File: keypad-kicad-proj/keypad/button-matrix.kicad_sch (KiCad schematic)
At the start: 36 parts, among them SW1 Cherry_MX, SW10 Cherry_MX, SW11 Cherry_MX, SW12 Cherry_MX, SW13 SW_SPST, SW14 SW_SPST, SW15 SW_SPST, SW16 SW_SPST, SW17 SW_SPST, SW18 SW_SPST, SW19 SW_SPST, SW2 Cherry_MX, SW20 SW_SPST, SW21 SW_SPST, SW22 SW_SPST, SW23 SW_SPST, SW24 SW_SPST, SW3 Cherry_MX, SW4 Cherry_MX, SW5 Cherry_MX, SW6 Cherry_MX, SW7 Cherry_MX, SW8 Cherry_MX, SW9 Cherry_MX

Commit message: rest of the schematic
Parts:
- renumbered D2 to D28, D6 to D29, D10 to D30, D3 to D31, D7 to D32, D11 to D33, D4 to D34, D8 to D35, D12 to D36, D5 to D37, D9 to D38, D13 to D39, SW1 to SW26, SW5 to SW27, SW9 to SW28, SW13 to SW29, SW15 to SW30, SW21 to SW31, SW2 to SW32, SW6 to SW33, SW10 to SW34, SW14 to SW35, SW16 to SW36, SW20 to SW37, SW3 to SW38, SW7 to SW39, SW11 to SW40, SW17 to SW41, SW18 to SW42, SW19 to SW43, SW4 to SW44, SW8 to SW45, SW12 to SW46, SW24 to SW47, SW23 to SW48, SW22 to SW49
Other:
- note added: "Button matrix (4x3)"
- title: (none) -> Keypad board
- moved on the sheet: D28, D29, D30, D31, D32, D33, D34, D35, D36, D37, D38, D39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

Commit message: keypad update
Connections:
- net Col_0 renamed col_0
- net Col_1 renamed col_1
- net Col_2 renamed col_2
- net Col_3 renamed col_3
- net Row_0 renamed row_0
- net Row_1 renamed row_1
- net Row_2 renamed row_2
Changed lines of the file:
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@@
     (effects (font (size 3 3) (thickness 0.6) bold) (justify left bottom))
   )
-  (global_label "Row_2" (shape input) (at 73.66 118.11 180) (fields_autoplaced)
+  (global_label "row_2" (shape input) (at 73.66 118.11 180) (fields_autoplaced)
     (effects (font (size 1.27 1.27)) (justify right))
-    (property "Intersheetrefs" "${INTERSHEET_REFS}" (at 64.7482 118.11 0)
+    (property "Intersheetrefs" "${INTERSHEET_REFS}" (at 65.232 118.11 0)
       (effects (font (size 1.27 1.27)) (justify right) hide)
     )
   )
-  (global_label "Col_3" (shape input) (at 226.06 54.61 0) (fields_autoplaced)
+  (global_label "col_3" (shape output) (at 226.06 54.61 0) (fields_autoplaced)
     (effects (font (size 1.27 1.27)) (justify left))
-    (property "Intersheetrefs" "${INTERSHEET_REFS}" (at 234.3065 54.61 0)
+    (property "Intersheetrefs" "${INTERSHEET_REFS}" (at 234.1251 54.61 0)
       (effects (font (size 1.27 1.27)) (justify left) hide)
     )
   )
-  (global_label "Col_2" (shape input) (at 187.96 54.61 0) (fields_autoplaced)
+  (global_label "col_2" (shape output) (at 187.96 54.61 0) (fields_autoplaced)
     (effects (font (size 1.27 1.27)) (justify left))
-    (property "Intersheetrefs" "${INTERSHEET_REFS}" (at 196.2065 54.61 0)
+    (property "Intersheetrefs" "${INTERSHEET_REFS}" (at 196.0251 54.61 0)
       (effects (font (size 1.27 1.27)) (justify left) hide)
     )
   )
-  (global_label "Row_1" (shape input) (at 73.66 90.17 180) (fields_autoplaced)
+  (global_label "row_1" (shape input) (at 73.66 90.17 180) (fields_autoplaced)
     (effects (font (size 1.27 1.27)) (justify right))
-    (property "Intersheetrefs" "${INTERSHEET_REFS}" (at 64.7482 90.17 0)
+    (property "Intersheetrefs" "${INTERSHEET_REFS}" (at 65.232 90.17 0)
       (effects (font (size 1.27 1.27)) (justify right) hide)
     )
   )
-  (global_label "Row_0" (shape input) (at 73.66 60.96 180) (fields_autoplaced)
+  (global_label "row_0" (shape input) (at 73.66 60.96 180) (fields_autoplaced)
     (effects (font (size 1.27 1.27)) (justify right))
-    (property "Intersheetrefs" "${INTERSHEET_REFS}" (at 64.7482 60.96 0)
+    (property "Intersheetrefs" "${INTERSHEET_REFS}" (at 65.232 60.96 0)
       (effects (font (size 1.27 1.27)) (justify right) hide)
     )
   )
-  (global_label "Col_1" (shape input) (at 148.59 54.61 0) (fields_autoplaced)
+  (global_label "col_1" (shape output) (at 148.59 54.61 0) (fields_autoplaced)
     (effects (font (size 1.27 1.27)) (justify left))
-    (property "Intersheetrefs" "${INTERSHEET_REFS}" (at 156.8365 54.61 0)
+    (property "Intersheetrefs" "${INTERSHEET_REFS}" (at 156.6551 54.61 0)
       (effects (font (size 1.27 1.27)) (justify left) hide)
     )
   )
-  (global_label "Col_0" (shape input) (at 109.22 54.61 0) (fields_autoplaced)
+  (global_label "col_0" (shape output) (at 109.22 54.61 0) (fields_autoplaced)
     (effects (font (size 1.27 1.27)) (justify left))
-    (property "Intersheetrefs" "${INTERSHEET_REFS}" (at 117.4665 54.61 0)
+    (property "Intersheetrefs" "${INTERSHEET_REFS}" (at 117.2851 54.61 0)
       (effects (font (size 1.27 1.27)) (justify left) hide)
     )

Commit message: footprints
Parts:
- D28, D29, D30, D31, D32, D33, D34, D35, D36, D37, D38, D39: footprint (none) -> Diode_SMD:D_SOD-123
- SW26, SW27, SW28, SW32, SW33, SW34, SW38, SW39, SW40, SW44, SW45, SW46: footprint SW_MX1A-E1NW_CHY -> PUT_RocketLab_other:MX1A-E1NW cherry mx blue rgb
- SW29, SW30, SW31, SW35, SW36, SW37, SW41, SW42, SW43, SW47, SW48, SW49: footprint (none) -> Button_Switch_THT:SW_PUSH-12mm_Wuerth-430476085716
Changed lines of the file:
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@@
       (effects (font (size 1.524 1.524)))
     )
-    (property "Footprint" "SW_MX1A-E1NW_CHY" (at 88.9 106.299 0)
+    (property "Footprint" "PUT_RocketLab_other:MX1A-E1NW cherry mx blue rgb" (at 88.9 106.299 0)
       (effects (font (size 1.524 1.524)) hide)
     )
@@
       (effects (font (size 1.524 1.524)))
     )
-    (property "Footprint" "SW_MX1A-E1NW_CHY" (at 205.74 106.299 0)
+    (property "Footprint" "PUT_RocketLab_other:MX1A-E1NW cherry mx blue rgb" (at 205.74 106.299 0)
       (effects (font (size 1.524 1.524)) hide)
     )
@@
       (effects (font (size 1.27 1.27)))
     )
-    (property "Footprint" "" (at 140.97 129.54 90)
+    (property "Footprint" "Diode_SMD:D_SOD-123" (at 140.97 129.54 90)
       (effects (font (size 1.27 1.27)) hide)
     )
@@
       (effects (font (size 1.27 1.27)))
     )
-    (property "Footprint" "" (at 88.9 138.43 0)
+    (property "Footprint" "Button_Switch_THT:SW_PUSH-12mm_Wuerth-430476085716" (at 88.9 138.43 0)
       (effects (font (size 1.27 1.27)) hide)
     )
@@
       (effects (font (size 1.27 1.27)))
     )
-    (property "Footprint" "" (at 205.74 110.49 0)
+    (property "Footprint" "Button_Switch_THT:SW_PUSH-12mm_Wuerth-430476085716" (at 205.74 110.49 0)
       (effects (font (size 1.27 1.27)) hide)
     )
@@
       (effects (font (size 1.27 1.27)))
     )
-    (property "Footprint" "" (at 167.64 138.43 0)
+    (property "Footprint" "Button_Switch_THT:SW_PUSH-12mm_Wuerth-430476085716" (at 167.64 138.43 0)
       (effects (font (size 1.27 1.27)) hide)
     )
@@
       (effects (font (size 1.524 1.524)))
     )
-    (property "Footprint" "SW_MX1A-E1NW_CHY" (at 88.9 134.239 0)
+    (property "Footprint" "PUT_RocketLab_other:MX1A-E1NW cherry mx blue rgb" (at 88.9 134.239 0)
       (effects (font (size 1.524 1.524)) hide)
     )
@@
       (effects (font (size 1.27 1.27)))
     )
-    (property "Footprint" "" (at 180.34 129.54 90)
+    (property "Footprint" "Diode_SMD:D_SOD-123" (at 180.34 129.54 90)
       (effects (font (size 1.27 1.27)) hide)
     )
@@
       (effects (font (size 1.27 1.27)))
     )
-    (property "Footprint" "" (at 128.27 110.49 0)
+    (property "Footprint" "Button_Switch_THT:SW_PUSH-12mm_Wuerth-430476085716" (at 128.27 110.49 0)
       (effects (font (size 1.27 1.27)) hide)
     )
@@
       (effects (font (size 1.27 1.27)))
     )
-    (property "Footprint" "" (at 128.27 138.43 0)
+    (property "Footprint" "Button_Switch_THT:SW_PUSH-12mm_Wuerth-430476085716" (at 128.27 138.43 0)
       (effects (font (size 1.27 1.27)) hide)
     )
@@
       (effects (font (size 1.524 1.524)))
     )
-    (property "Footprint" "SW_MX1A-E1NW_CHY" (at 167.64 77.089 0)
+    (property "Footprint" "PUT_RocketLab_other:MX1A-E1NW cherry mx blue rgb" (at 167.64 77.089 0)
       (effects (font (size 1.524 1.524)) hide)
     )
@@
       (effects (font (size 1.524 1.524)))
     )
-    (property "Footprint" "SW_MX1A-E1NW_CHY" (at 205.74 134.239 0)
+    (property "Footprint" "PUT_RocketLab_other:MX1A-E1NW cherry mx blue rgb" (at 205.74 134.239 0)
       (effects (font (size 1.524 1.524)) hide)
     )
@@
       (effects (font (size 1.27 1.27)))
     )
-    (property "Footprint" "" (at 167.64 110.49 0)
+    (property "Footprint" "Button_Switch_THT:SW_PUSH-12mm_Wuerth-430476085716" (at 167.64 110.49 0)
       (effects (font (size 1.27 1.27)) hide)
     )
@@
       (effects (font (size 1.27 1.27)))
     )
-    (property "Footprint" "" (at 218.44 129.54 90)
+    (property "Footprint" "Diode_SMD:D_SOD-123" (at 218.44 129.54 90)
       (effects (font (size 1.27 1.27)) hide)
     )
@@
     )
   )
-  (symbol (lib_id "PUT_RocketLab_misc:Cherry_MX") (at 120.65 101.6 0) (unit 1)
+  (symbol (lib_name "Cherry_MX_1") (lib_id "PUT_RocketLab_misc:Cherry_MX") (at 120.65 101.6 0) (unit 1)
     (in_bom yes) (on_board yes) (dnp no) (fields_autoplaced)
     (property "Reference" "SW33" (at 128.27 93.98 0)
@@
       (effects (font (size 1.524 1.524)))
     )
-    (property "Footprint" "SW_MX1A-E1NW_CHY" (at 128.27 106.299 0)
+    (property "Footprint" "PUT_RocketLab_other:MX1A-E1NW cherry mx blue rgb" (at 128.27 106.299 0)
       (effects (font (size 1.524 1.524)) hide)
     )
@@
       (effects (font (size 1.27 1.27)))
     )
-    (property "Footprint" "" (at 140.97 101.6 90)
+    (property "Footprint" "Diode_SMD:D_SOD-123" (at 140.97 101.6 90)
       (effects (font (size 1.27 1.27)) hide)
     )
@@
       (effects (font (size 1.27 1.27)))
     )
-    (property "Footprint" "" (at 88.9 110.49 0)
+    (property "Footprint" "Button_Switch_THT:SW_PUSH-12mm_Wuerth-430476085716" (at 88.9 110.49 0)
       (effects (font (size 1.27 1.27)) hide)
     )
@@
       (effects (font (size 1.27 1.27)))
     )
-    (property "Footprint" "" (at 101.6 129.54 90)
+    (property "Footprint" "Diode_SMD:D_SOD-123" (at 101.6 129.54 90)
       (effects (font (size 1.27 1.27)) hide)
     )
@@
       (effects (font (size 1.27 1.27)))
     )
-    (property "Footprint" "" (at 101.6 72.39 90)
+    (property "Footprint" "Diode_SMD:D_SOD-123" (at 101.6 72.39 90)
       (effects (font (size 1.27 1.27)) hide)
     )
@@
       (effects (font (size 1.27 1.27)))
     )
-    (property "Footprint" "" (at 128.27 81.28 0)
+    (property "Footprint" "Button_Switch_THT:SW_PUSH-12mm_Wuerth-430476085716" (at 128.27 81.28 0)
       (effects (font (size 1.27 1.27)) hide)
     )
@@
       (effects (font (size 1.524 1.524)))
     )
-    (property "Footprint" "SW_MX1A-E1NW_CHY" (at 205.74 77.089 0)
+    (property "Footprint" "PUT_RocketLab_other:MX1A-E1NW cherry mx blue rgb" (at 205.74 77.089 0)
       (effects (font (size 1.524 1.524)) hide)
     )
@@
       (effects (font (size 1.524 1.524)))
     )
-    (property "Footprint" "SW_MX1A-E1NW_CHY" (at 128.27 134.239 0)
+    (property "Footprint" "PUT_RocketLab_other:MX1A-E1NW cherry mx blue rgb" (at 128.27 134.239 0)
       (effects (font (size 1.524 1.524)) hide)
     )
@@
       (effects (font (size 1.524 1.524)))
     )
-    (property "Footprint" "SW_MX1A-E1NW_CHY" (at 167.64 134.239 0)
+    (property "Footprint" "PUT_RocketLab_other:MX1A-E1NW cherry mx blue rgb" (at 167.64 134.239 0)
       (effects (font (size 1.524 1.524)) hide)
     )
@@
       (effects (font (size 1.27 1.27)))
     )
-    (property "Footprint" "" (at 180.34 72.39 90)
+    (property "Footprint" "Diode_SMD:D_SOD-123" (at 180.34 72.39 90)
       (effects (font (size 1.27 1.27)) hide)
     )
@@
       (effects (font (size 1.27 1.27)))
     )
-    (property "Footprint" "" (at 88.9 81.28 0)
+    (property "Footprint" "Button_Switch_THT:SW_PUSH-12mm_Wuerth-430476085716" (at 88.9 81.28 0)
       (effects (font (size 1.27 1.27)) hide)
     )
@@
       (effects (font (size 1.27 1.27)))
     )
-    (property "Footprint" "" (at 205.74 81.28 0)
+    (property "Footprint" "Button_Switch_THT:SW_PUSH-12mm_Wuerth-430476085716" (at 205.74 81.28 0)
       (effects (font (size 1.27 1.27)) hide)
     )
@@
       (effects (font (size 1.27 1.27)))
     )
-    (property "Footprint" "" (at 218.44 101.6 90)
+    (property "Footprint" "Diode_SMD:D_SOD-123" (at 218.44 101.6 90)
       (effects (font (size 1.27 1.27)) hide)
     )
@@
       (effects (font (size 1.27 1.27)))
     )
-    (property "Footprint" "" (at 180.34 101.6 90)
+    (property "Footprint" "Diode_SMD:D_SOD-123" (at 180.34 101.6 90)
       (effects (font (size 1.27 1.27)) hide)
     )
@@
       (effects (font (size 1.524 1.524)))
     )
-    (property "Footprint" "SW_MX1A-E1NW_CHY" (at 128.27 77.089 0)
+    (property "Footprint" "PUT_RocketLab_other:MX1A-E1NW cherry mx blue rgb" (at 128.27 77.089 0)
       (effects (font (size 1.524 1.524)) hide)
     )
@@
       (effects (font (size 1.27 1.27)))
     )
-    (property "Footprint" "" (at 140.97 72.39 90)
+    (property "Footprint" "Diode_SMD:D_SOD-123" (at 140.97 72.39 90)
       (effects (font (size 1.27 1.27)) hide)
     )
@@
       (effects (font (size 1.524 1.524)))
     )
-    (property "Footprint" "SW_MX1A-E1NW_CHY" (at 88.9 77.089 0)
+    (property "Footprint" "PUT_RocketLab_other:MX1A-E1NW cherry mx blue rgb" (at 88.9 77.089 0)
       (effects (font (size 1.524 1.524)) hide)
     )
@@
       (effects (font (size 1.524 1.524)))
     )
-    (property "Footprint" "SW_MX1A-E1NW_CHY" (at 167.64 106.299 0)
+    (property "Footprint" "PUT_RocketLab_other:MX1A-E1NW cherry mx blue rgb" (at 167.64 106.299 0)
       (effects (font (size 1.524 1.524)) hide)
     )
@@
       (effects (font (size 1.27 1.27)))
     )
-    (property "Footprint" "" (at 218.44 72.39 90)
+    (property "Footprint" "Diode_SMD:D_SOD-123" (at 218.44 72.39 90)
       (effects (font (size 1.27 1.27)) hide)
     )
@@
       (effects (font (size 1.27 1.27)))
     )
-    (property "Footprint" "" (at 167.64 81.28 0)
+    (property "Footprint" "Button_Switch_THT:SW_PUSH-12mm_Wuerth-430476085716" (at 167.64 81.28 0)
       (effects (font (size 1.27 1.27)) hide)
     )
@@
       (effects (font (size 1.27 1.27)))
     )
-    (property "Footprint" "" (at 205.74 138.43 0)
+    (property "Footprint" "Button_Switch_THT:SW_PUSH-12mm_Wuerth-430476085716" (at 205.74 138.43 0)
       (effects (font (size 1.27 1.27)) hide)
     )
@@
       (effects (font (size 1.27 1.27)))
     )
-    (property "Footprint" "" (at 101.6 101.6 90)
-      (effects (font (size 1.27 1.27)) hide)
-    )
+    (property "Footprint" "Diode_SMD:D_SOD-123" (at 101.6 101.6 90)
+      (effects (font (size 1.27 1.27)) hide)
+    )

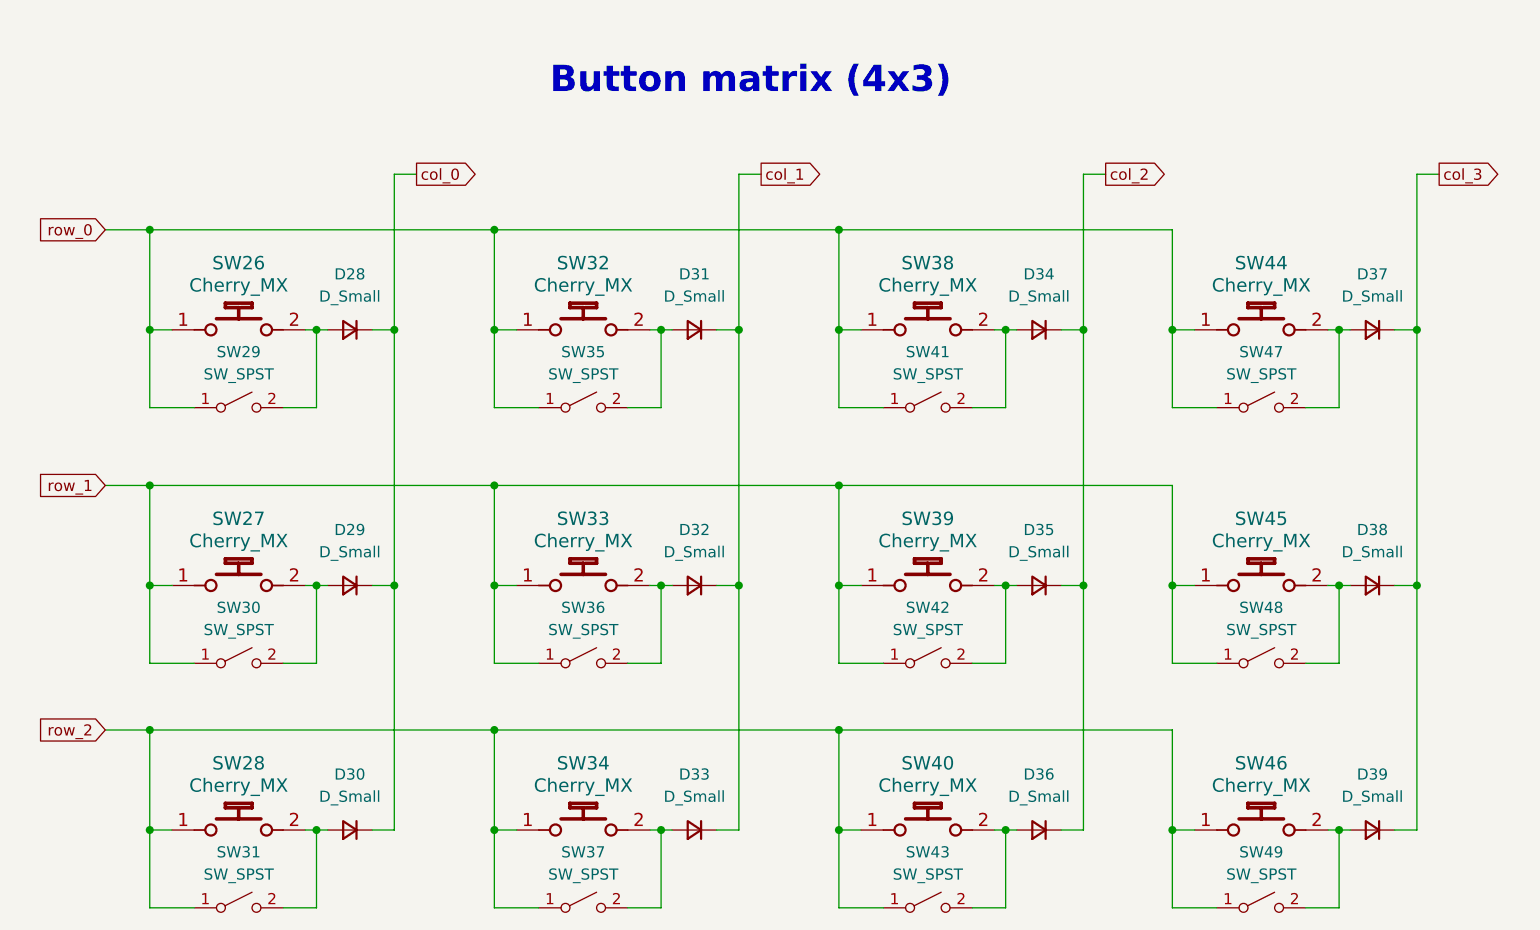
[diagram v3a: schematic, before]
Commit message: rm keypad 2ndary btns
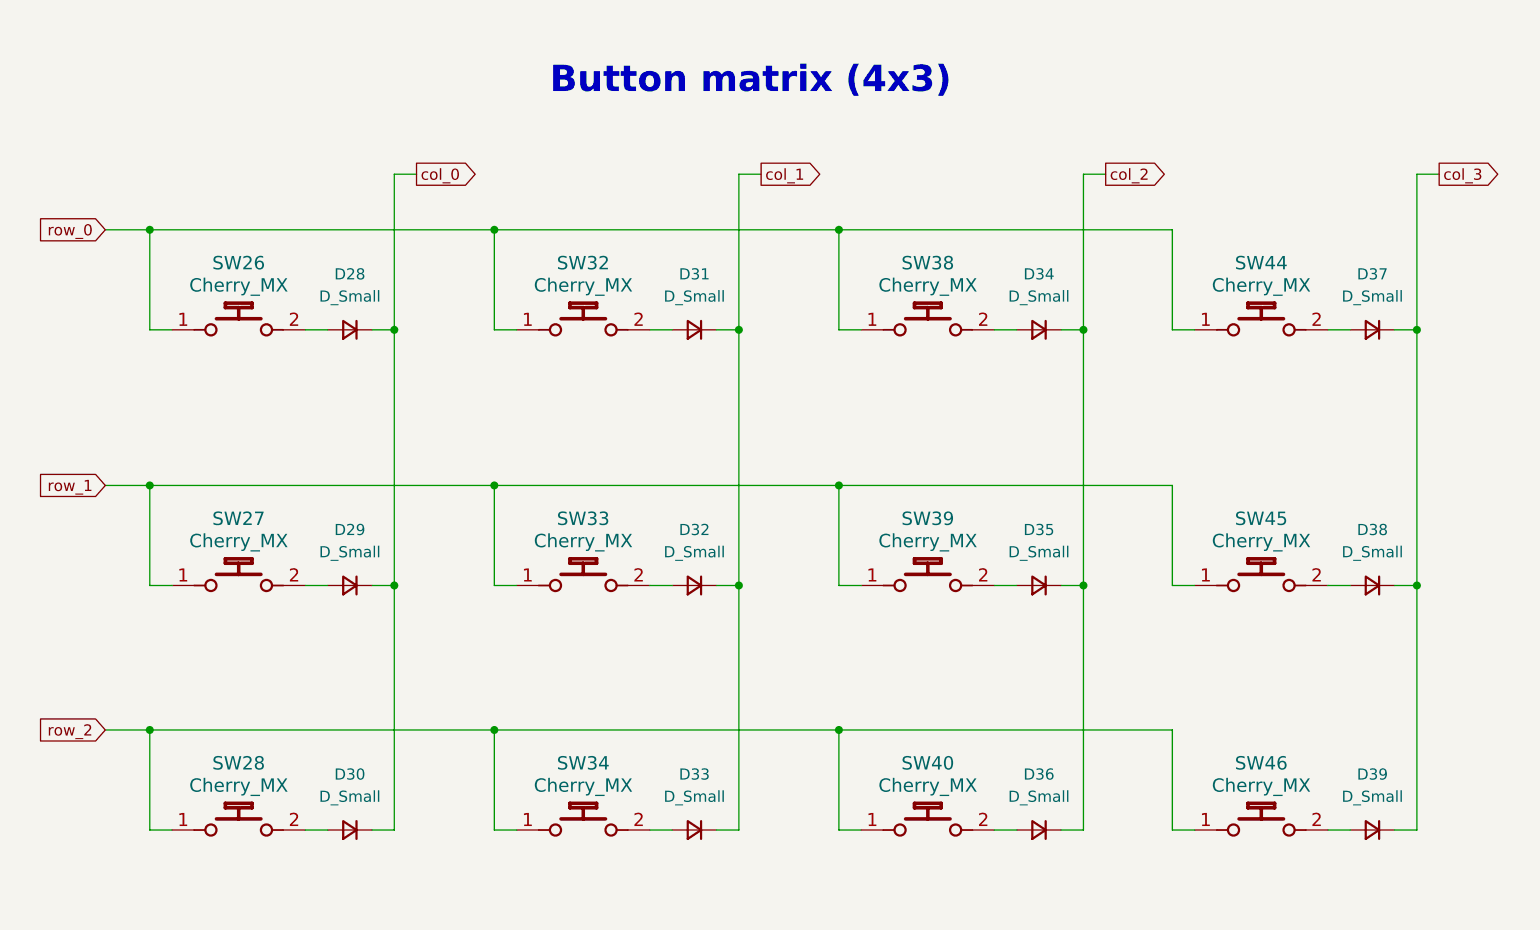
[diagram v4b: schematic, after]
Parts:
- removed SW29, SW30, SW31, SW35, SW36, SW37, SW41, SW42, SW43, SW47, SW48, SW49: SW_SPST, Button_Switch_THT:SW_PUSH-12mm_Wuerth-430476085716, symbol Switch:SW_SPST
